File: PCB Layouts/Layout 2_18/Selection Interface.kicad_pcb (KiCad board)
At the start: 4 copper layers, 110 x 90 mm, 95 parts

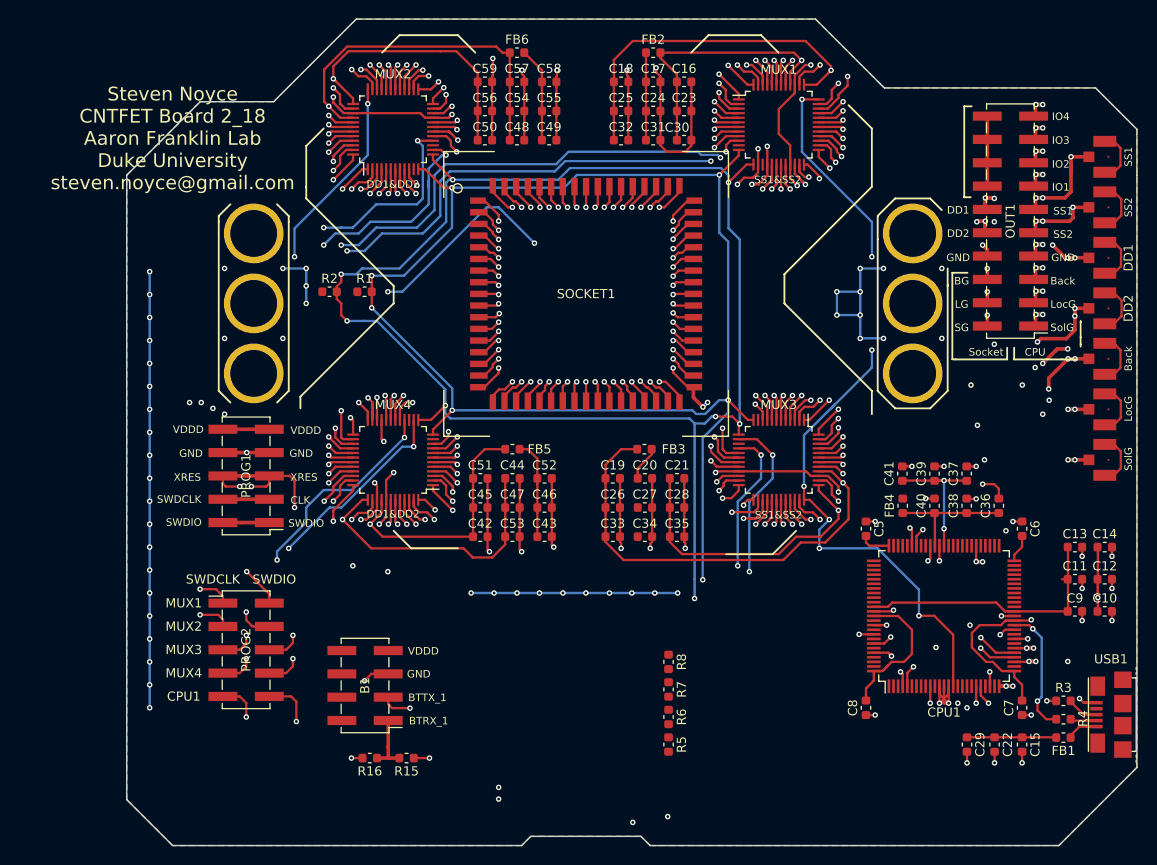
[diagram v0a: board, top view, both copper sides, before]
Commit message: Finished moving CPU1 and re-connecting all signals. Started arranging external resistors and moved bluetooth connector even closer
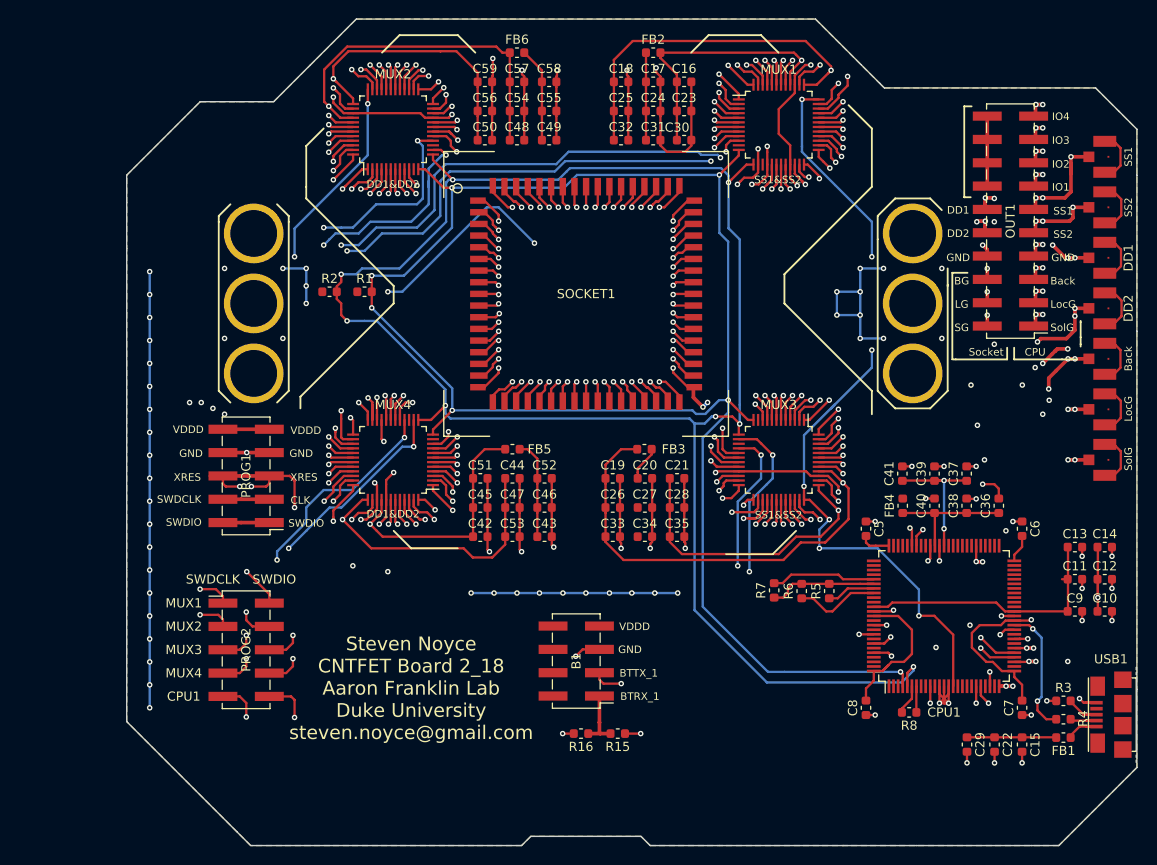
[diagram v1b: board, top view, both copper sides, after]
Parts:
- R5: value R -> 100M
- R6, R8: value R -> 1M
- R7: value R -> 10k
- moved R8 26.8 mm to (235.2, 145.5), turned to 0 degrees
- moved R5 24.2 mm to (226.5, 132.3), turned to 90 degrees
- moved B1 23.2 mm to (198.9, 139.9)
- moved R15 23.2 mm to (203.5, 147.8)
- moved R16 23.2 mm to (199.5, 147.8)
- moved R6 20.0 mm to (223.5, 132.3), turned to 90 degrees
- moved R7 15.8 mm to (220.5, 132.2)
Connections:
- net Net-(CPU1-Pad16) renamed OPAMP_VOUT
- net Net-(CPU1-Pad8) renamed OPAMP_Vminus
- net Net-(CPU1-Pad9) renamed OPAMP_Vplus
- CPU1 pad 6: Net-(CPU1-Pad6) -> Gate_R1M_Low
- CPU1 pad 7: Net-(CPU1-Pad7) -> Gate_R1M_High
- CPU1 pad 80: Net-(CPU1-Pad80) -> TIA_R10k
- CPU1 pad 81: Net-(CPU1-Pad81) -> TIA_R_COMMON
- CPU1 pad 82: Net-(CPU1-Pad82) -> TIA_R100M
- CPU1 pad 83: Net-(CPU1-Pad83) -> TIA_R1M
- R5 pad 1: Net-(CPU1-Pad83) -> TIA_R100M
- R5 pad 2: Net-(CPU1-Pad84) -> TIA_R_COMMON
- R6 pad 1: Net-(CPU1-Pad81) -> TIA_R1M
- R6 pad 2: Net-(CPU1-Pad82) -> TIA_R_COMMON
- R7 pad 1: Net-(CPU1-Pad79) -> TIA_R10k
- R7 pad 2: Net-(CPU1-Pad80) -> TIA_R_COMMON
- R8 pad 1: Net-(CPU1-Pad77) -> Gate_R1M_Low
- R8 pad 2: Net-(CPU1-Pad78) -> Gate_R1M_High
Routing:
- net I2C0_SDA: track 166.1 -> 195.4 mm, vias 9 -> 8
- net I2C0_SCL: track 156.7 -> 184.1 mm, vias 8 -> 7
- net SWDCLK5: track 73.8 -> 90.2 mm, vias 3 -> 2
- net BT1_RX: track 66.1 -> 49.8 mm, vias 4 -> 2
- net SWDIO5: track 68.7 -> 82.8 mm, vias 3 -> 2
- net BT1_TX: track 69.0 -> 56.0 mm, vias 4 -> 2
- net TIA_R_COMMON: track 0.00 -> 11.8 mm
- net TIA_R10k: track 0.00 -> 11.4 mm
- net TIA_R1M: track 0.00 -> 9.27 mm
- net TIA_R100M: track 0.00 -> 5.30 mm
- net Gate_R1M_Low: track 0.00 -> 3.30 mm
- net Gate_R1M_High: track 0.00 -> 2.86 mm
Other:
- outline, holes or cut-outs redrawn

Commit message: Added external op-amp schematic and footprint. Continuing to make progress in slimming down the PCB
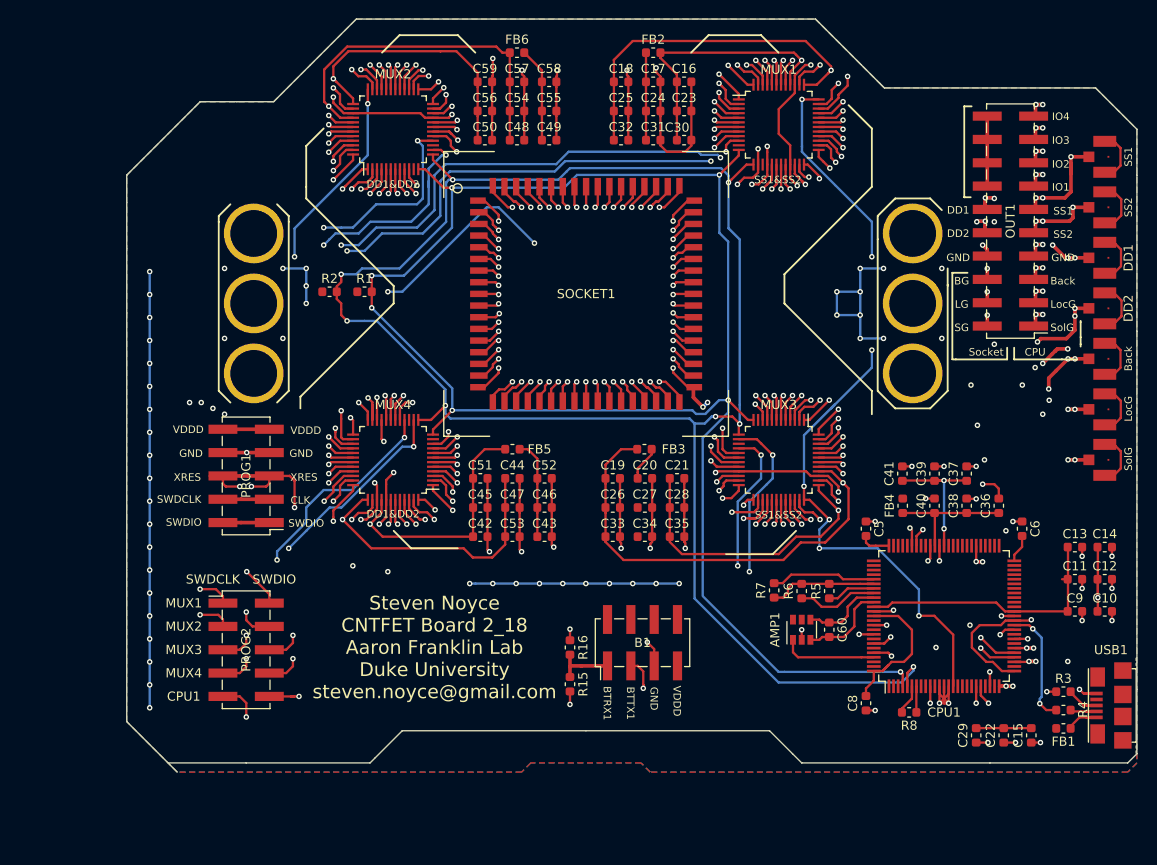
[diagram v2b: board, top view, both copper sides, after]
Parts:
- removed C7: 0.1uF, Capacitor_SMD:C_0603_1608Metric
- added AMP1: OPA363, Package_TO_SOT_SMD:SOT-23-6, F.Cu at (223.5, 136.5)
- added C60: 1pF, Capacitor_SMD:C_0603_1608Metric, F.Cu at (226.5, 136.5)
- moved R16 9.45 mm to (198.3, 138.4), turned to 90 degrees
- moved B1 7.49 mm to (206.2, 137.9), turned to 90 degrees
- moved R15 7.48 mm to (198.3, 142.4), turned to 90 degrees
- moved C15 1.41 mm to (248.5, 148.0)
- moved C22 1.41 mm to (245.5, 148.0)
- moved C29 1.41 mm to (242.5, 148.0)
- moved FB1 1.00 mm to (252.0, 147.2)
- moved R3 1.00 mm to (252.0, 143.2)
- moved R4 1.00 mm to (252.0, 145.2)
- moved USB1 1.00 mm to (258.5, 144.7)
- moved C8 0.50 mm to (230.5, 144.5)
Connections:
- net OPAMP_VOUT renamed Net-(CPU1-Pad16)
- net OPAMP_Vminus renamed Net-(CPU1-Pad8)
- net OPAMP_Vplus renamed Net-(CPU1-Pad9)
- CPU1 pad 84: Net-(CPU1-Pad84) -> AMP1_Vminus
- CPU1 pad 85: Net-(CPU1-Pad85) -> AMP1_Vplus
- CPU1 pad 97: Net-(CPU1-Pad97) -> AMP1_VOUT
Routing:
- net AMP1_VOUT: track 0.00 -> 10.4 mm
- net BT1_RX: track 49.8 -> 60.0 mm
- net AMP1_Vplus: track 0.00 -> 9.70 mm
- net AMP1_Vminus: track 0.00 -> 8.74 mm
- net VDDD: track 173.9 -> 166.1 mm
- net BT1_TX: track 56.0 -> 54.3 mm
- net USBDM_C1: track 14.1 -> 12.9 mm
- net USBDP_C1: track 13.1 -> 11.9 mm
- net DD1: track 246.6 -> 245.5 mm
- net DD2: track 239.6 -> 238.7 mm
- net I2C0_SCL: track 184.1 -> 183.3 mm
- net SWDIO5: track 82.8 -> 82.1 mm
- net I2C0_SDA: track 195.4 -> 194.7 mm
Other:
- board size 110 x 90 mm -> 110 x 82 mm
- board text added: "BTRX1"
- board text added: "BTTX1"
- board text removed: "BTRX_1"
- board text removed: "BTTX_1"

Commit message: Converted all CPU gate channels to a single CPU gate channel. Also continued shrinking and cleaning up routing
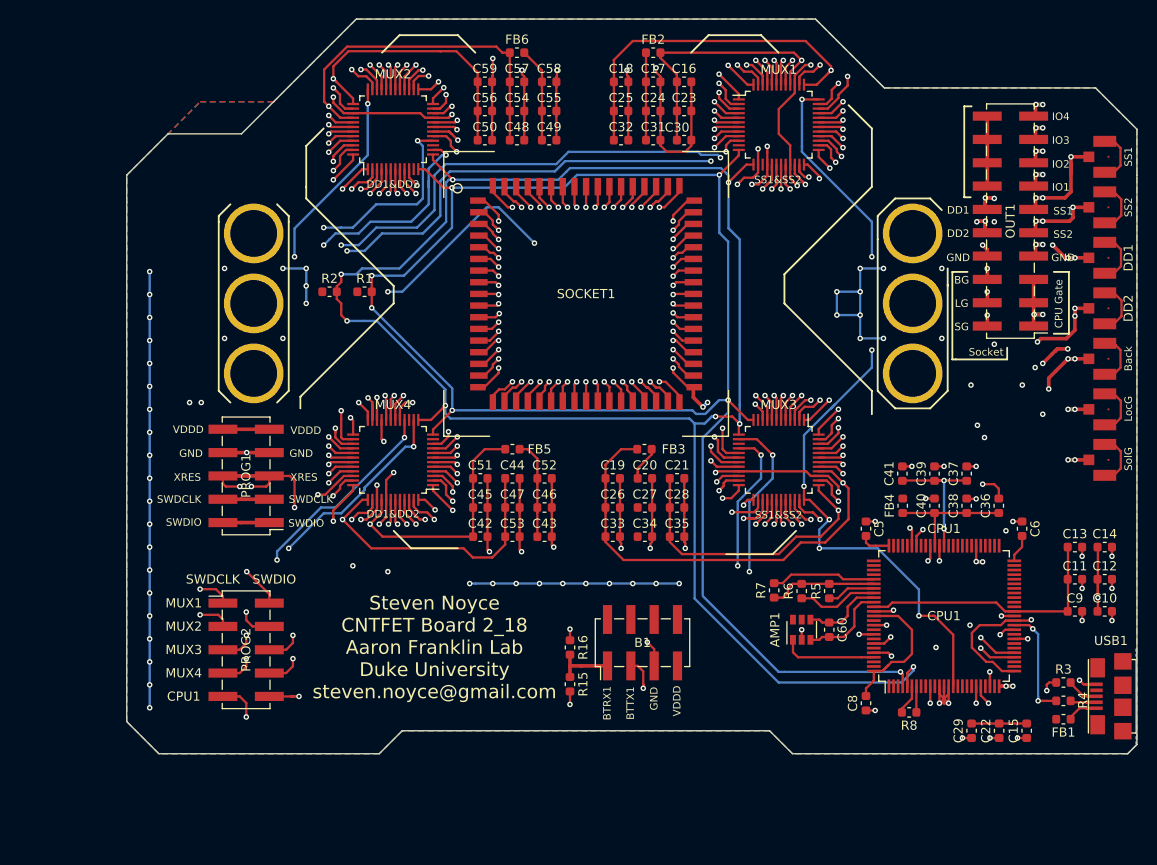
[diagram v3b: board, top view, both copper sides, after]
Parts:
- moved FB1 1.00 mm to (252.0, 146.2)
- moved R3 1.00 mm to (252.0, 142.2)
- moved R4 1.00 mm to (252.0, 144.2)
- moved USB1 1.00 mm to (258.5, 143.7)
- moved C15 0.71 mm to (248.0, 147.5)
- moved C22 0.71 mm to (245.0, 147.5)
- moved C29 0.71 mm to (242.0, 147.5)
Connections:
- CPU1 pad 25: SolutionGate -> Gate
- CPU1 pad 28: LocalGates -> Net-(CPU1-Pad28)
- CPU1 pad 31: BackGate -> Net-(CPU1-Pad31)
- OUT1 pad 1: SolutionGate -> Gate
- OUT1 pad 3: LocalGates -> Gate
- OUT1 pad 5: BackGate -> Gate
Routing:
- net Gate: track 0.00 -> 57.2 mm, vias 0 -> 4
- net LocalGates: track 54.6 -> 0.00 mm, vias 5 -> 0
- net BackGate: track 53.2 -> 0.00 mm, vias 5 -> 0
- net SolutionGate: track 52.2 -> 0.00 mm, vias 4 -> 0
- net SWDIO2: track 76.7 -> 90.7 mm, vias 4 -> 3
- net SWDIO1: track 107.8 -> 121.0 mm, vias 6 -> 5
- net SWDCLK2: track 84.6 -> 87.3 mm
- net SWDCLK1: track 119.8 -> 122.1 mm
- net SolutionGate_Socket: track 84.2 -> 82.8 mm
- net SWDCLK4: track 39.6 -> 38.7 mm
- net USBDP_C1: track 11.9 -> 12.7 mm
- net VCCD_C1: track 29.4 -> 28.7 mm
- net USBDM_C1: track 12.9 -> 12.2 mm
- net GND: track 301.1 -> 300.5 mm
- net DD1: track 245.5 -> 245.0 mm
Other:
- board size 110 x 82 mm -> 110 x 80 mm
- board text added: "CPU Gate"
- board text removed: "CLK"
- board text removed: "CPU"

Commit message: Continuing to shrink layout 2_18
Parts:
- moved B1 26.0 mm to (180.1, 137.9)
- moved R15 26.0 mm to (172.2, 142.4)
- moved R16 26.0 mm to (172.2, 138.4)
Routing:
- net BT1_TX: track 54.3 -> 81.9 mm
- net BT1_RX: track 60.0 -> 86.7 mm
- net SWDCLK5: track 90.2 -> 93.8 mm
- net SWDIO5: track 81.8 -> 84.6 mm
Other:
- board size 110 x 80 mm -> 107.5 x 80 mm

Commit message: Starting to put on the finishing touches to Layout 2_18
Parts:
- moved C53 6.36 mm to (192.0, 120.0)
- moved C44 6.35 mm to (192.0, 126.4)
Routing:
- net GND: track 300.5 -> 422.9 mm, vias 106 -> 149
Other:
- outline, holes or cut-outs redrawn

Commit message: Generated gerber files for Layout 2_18
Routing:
- net GND: track 422.9 -> 430.5 mm, vias 149 -> 153
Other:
- outline, holes or cut-outs redrawn
- board text added: "Steven Noyce & JLD CNTFET Board 2_18 Aaron Franklin Lab Duke University steven.noyce@gmail.com"
- board text removed: "Steven Noyce CNTFET Board 2_18 Aaron Franklin Lab Duke University steven.noyce@gmail.com"
